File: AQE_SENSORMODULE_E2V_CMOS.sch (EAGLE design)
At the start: 29 parts, among them J1 440055-4, J2 AVR_SPI_PRG_6NS, U1 V_REG_LDOSMD, U2 V_REG_LDOSMD

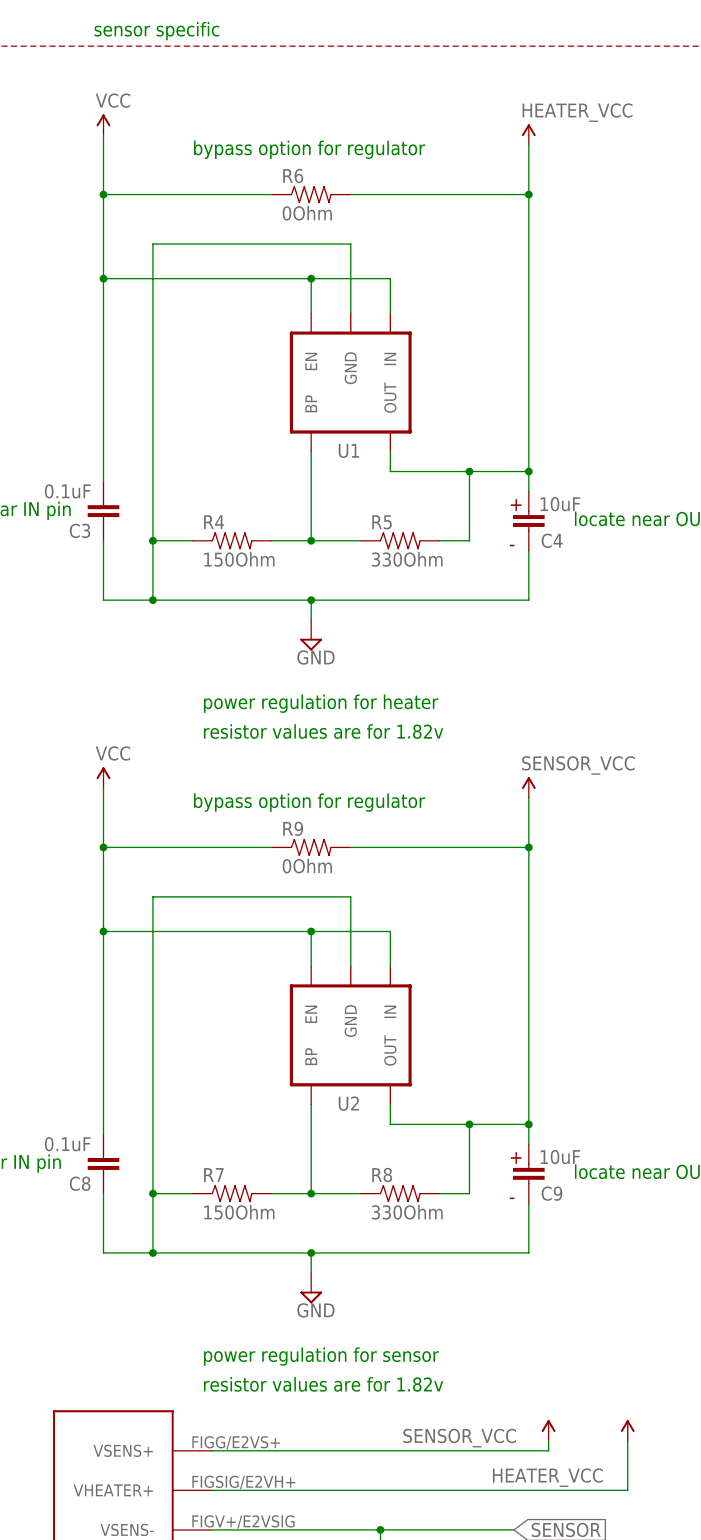
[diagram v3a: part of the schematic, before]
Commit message: minor changes in routing and component placement for improved decoupling, more representative values for resistors, and minor changes to silk screen
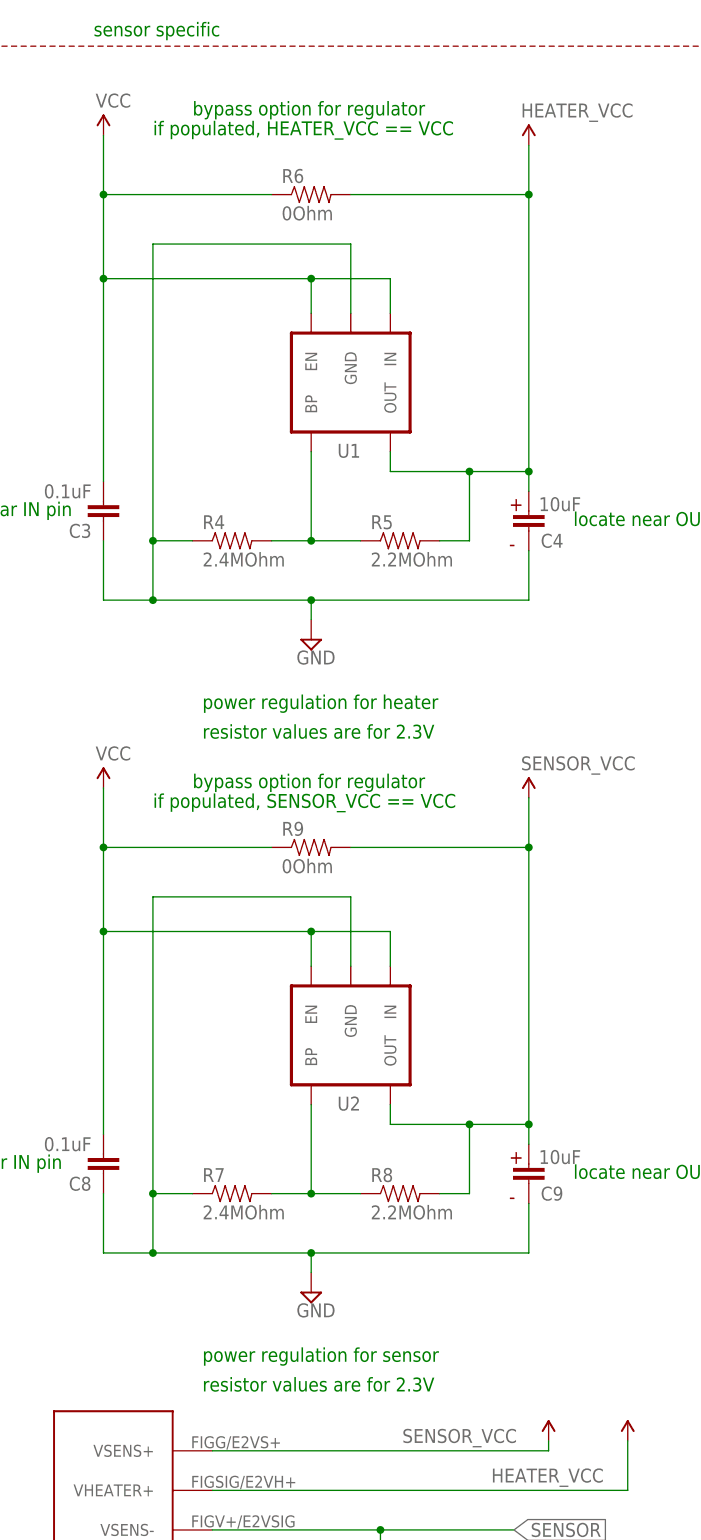
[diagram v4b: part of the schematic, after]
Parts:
- R4, R7: value 150Ohm -> 2.4MOhm
- R5, R8: value 330Ohm -> 2.2MOhm
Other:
- note added: "if populated, HEATER_VCC == VCC"
- note added: "if populated, SENSOR_VCC == VCC"
- note added: "resistor values are for 2.3V"
- note removed: "resistor values are for 1.82v"
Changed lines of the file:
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@@
 <setting verticaltext="up"/>
 </settings>
-<grid distance="0.05" unitdist="inch" unit="inch" style="lines" multiple="1" display="no" altdistance="0.01" altunitdist="inch" altunit="inch"/>
+<grid distance="0.1" unitdist="inch" unit="inch" style="lines" multiple="1" display="no" altdistance="0.01" altunitdist="inch" altunit="inch"/>
 <layers>
 <layer number="1" name="Top" color="4" fill="1" visible="no" active="no"/>
@@
 <part name="P+6" library="SparkFun" deviceset="VCC" device=""/>
 <part name="C6" library="SparkFun" deviceset="CAP" device="0603-CAP" value="0.1uF"/>
-<part name="R4" library="SparkFun" deviceset="RESISTOR" device="0805-RES" value="150Ohm"/>
-<part name="R5" library="SparkFun" deviceset="RESISTOR" device="0805-RES" value="330Ohm"/>
+<part name="R4" library="SparkFun" deviceset="RESISTOR" device="0805-RES" value="2.4MOhm"/>
+<part name="R5" library="SparkFun" deviceset="RESISTOR" device="0805-RES" value="2.2MOhm"/>
 <part name="C7" library="SparkFun" deviceset="CAP" device="0603-CAP" value="0.1uF"/>
 <part name="SUPPLY8" library="supply2" deviceset="GND" device=""/>
@@
 <part name="C9" library="wicked-device" deviceset="EEE-1EA100WR" device="" value="10uF"/>
 <part name="R9" library="SparkFun" deviceset="RESISTOR" device="0805-RES" value="0Ohm"/>
-<part name="R7" library="SparkFun" deviceset="RESISTOR" device="0805-RES" value="150Ohm"/>
-<part name="R8" library="SparkFun" deviceset="RESISTOR" device="0805-RES" value="330Ohm"/>
+<part name="R7" library="SparkFun" deviceset="RESISTOR" device="0805-RES" value="2.4MOhm"/>
+<part name="R8" library="SparkFun" deviceset="RESISTOR" device="0805-RES" value="2.2MOhm"/>
 <part name="U2" library="SparkFun" deviceset="V_REG_LDO" device="SMD"/>
 <part name="JP1" library="SparkFun" deviceset="STAND-OFF" device=""/>
@@
 <wire x1="152.4" y1="266.7" x2="40.64" y2="266.7" width="0.1524" layer="94" style="shortdash"/>
 <text x="67.31" y="267.97" size="1.778" layer="91">sensor specific</text>
-<text x="80.01" y="252.73" size="1.778" layer="91">bypass option for regulator</text>
+<text x="80.01" y="257.81" size="1.778" layer="91">bypass option for regulator</text>
 <text x="271.78" y="90.17" size="1.778" layer="91">programming header</text>
 <text x="76.2" y="12.7" size="1.778" layer="91">resistor values are sensor dependent</text>
@@
 <text x="158.75" y="120.65" size="1.778" layer="91">locate near VCC pin</text>
 <text x="124.46" y="207.01" size="1.778" layer="96">10uF</text>
-<text x="81.28" y="177.8" size="1.778" layer="91">resistor values are for 1.82v</text>
+<text x="81.28" y="177.8" size="1.778" layer="91">resistor values are for 2.3V</text>
 <text x="267.97" y="181.61" size="1.778" layer="91">locate near AREF pin</text>
 <text x="81.28" y="97.79" size="1.778" layer="91">power regulation for sensor</text>
-<text x="80.01" y="168.91" size="1.778" layer="91">bypass option for regulator</text>
+<text x="80.01" y="171.45" size="1.778" layer="91">bypass option for regulator</text>
 <text x="124.46" y="123.19" size="1.778" layer="96">10uF</text>
-<text x="81.28" y="93.98" size="1.778" layer="91">resistor values are for 1.82v</text>
+<text x="81.28" y="93.98" size="1.778" layer="91">resistor values are for 2.3V</text>
 <text x="45.085" y="206.375" size="1.778" layer="91">locate near IN pin</text>
 <text x="128.905" y="205.105" size="1.778" layer="91">locate near OUT pin</text>
@@
 <text x="128.905" y="121.285" size="1.778" layer="91">locate near OUT pin</text>
 <text x="359.41" y="146.685" size="1.778" layer="91">standoffs</text>
+<text x="74.93" y="255.27" size="1.778" layer="91">if populated, HEATER_VCC == VCC</text>
+<text x="74.93" y="168.91" size="1.778" layer="91">if populated, SENSOR_VCC == VCC</text>
 </plain>
 <instances>

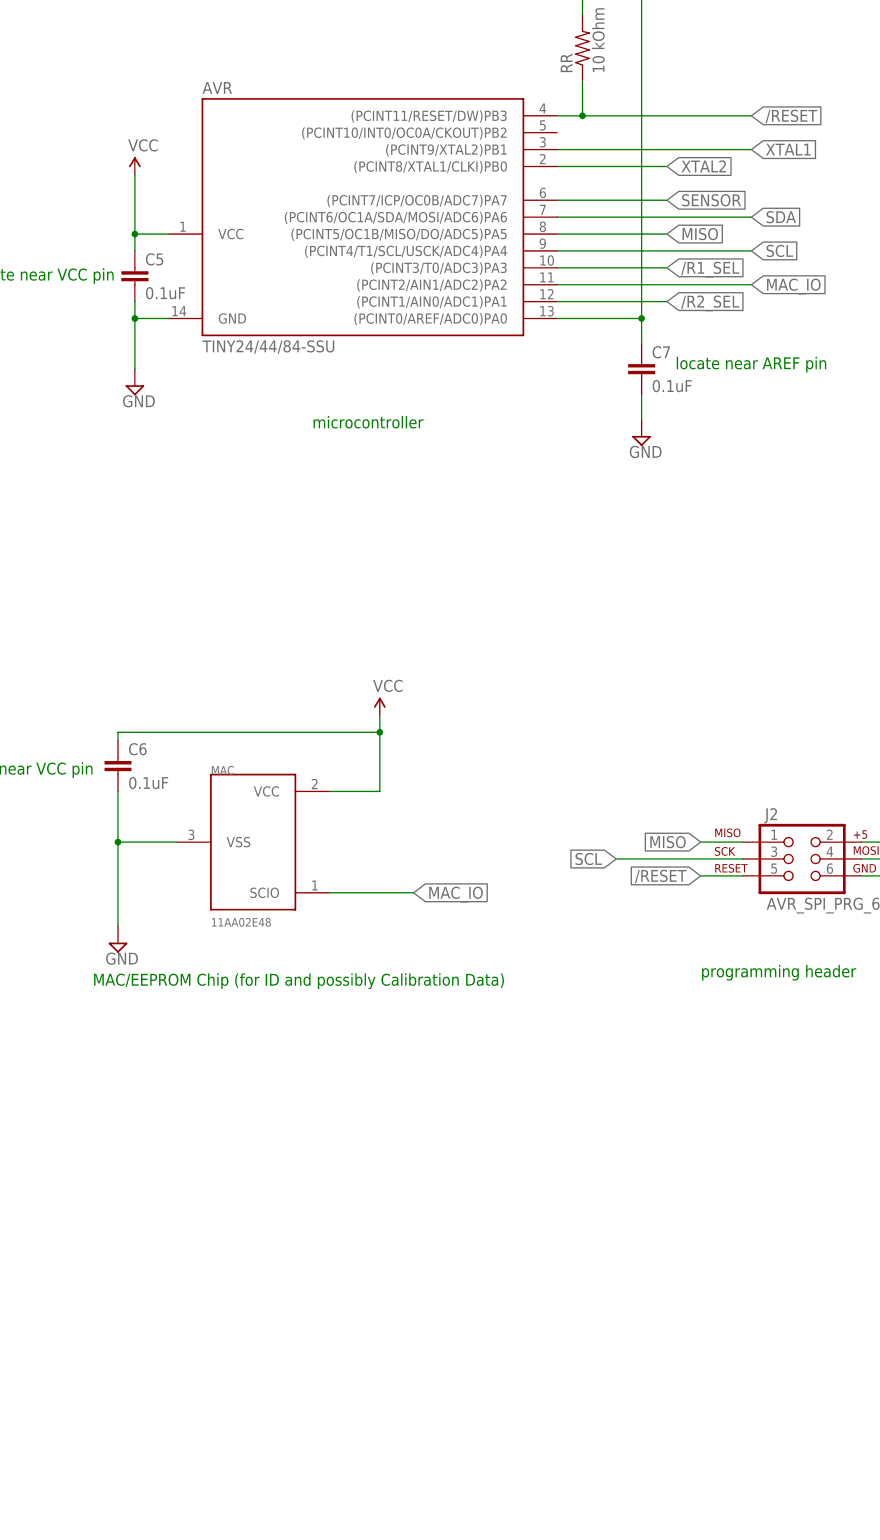
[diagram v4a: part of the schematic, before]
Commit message: last changes before switching heater approach to feedback controlled and changing microcontroller
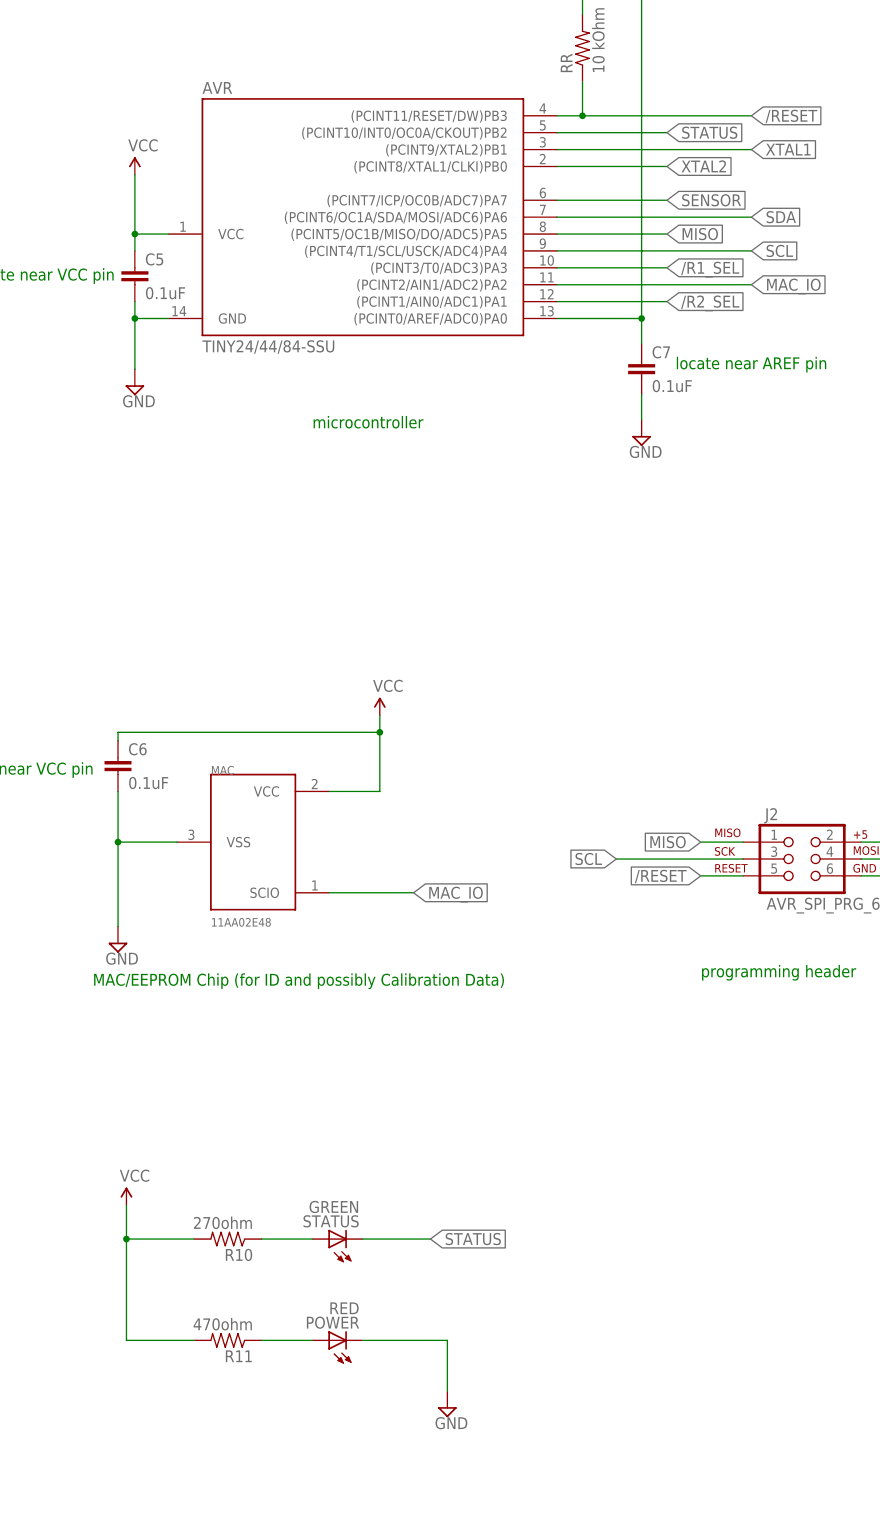
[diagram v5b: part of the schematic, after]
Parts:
- added POWER: RED, adafruit:LEDCHIPLED_0805
- added R10: 270ohm, SparkFun:RESISTOR0805-RES
- added R11: 470ohm, SparkFun:RESISTOR0805-RES
- added STATUS: GREEN, adafruit:LEDCHIPLED_0805
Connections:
- new net N$3: POWER.A, R11.1
- new net N$4: R10.1, STATUS.A
- new net STATUS: AVR.(PCINT10/INT0/OC0A/CKOUT)PB2, STATUS.C
- net GND: now also POWER.C
- net VCC: now also R10.2, R11.2
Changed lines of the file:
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@@
 <part name="JP1" library="SparkFun" deviceset="STAND-OFF" device=""/>
 <part name="JP2" library="SparkFun" deviceset="STAND-OFF" device=""/>
+<part name="STATUS" library="adafruit" deviceset="LED" device="CHIPLED_0805" value="GREEN"/>
+<part name="R10" library="SparkFun" deviceset="RESISTOR" device="0805-RES" value="270ohm"/>
+<part name="P+8" library="SparkFun" deviceset="VCC" device=""/>
+<part name="POWER" library="adafruit" deviceset="LED" device="CHIPLED_0805" value="RED"/>
+<part name="R11" library="SparkFun" deviceset="RESISTOR" device="0805-RES" value="470ohm"/>
+<part name="SUPPLY10" library="supply2" deviceset="GND" device=""/>
 </parts>
 <sheets>
@@
 <instance part="JP1" gate="G$1" x="361.95" y="152.4"/>
 <instance part="JP2" gate="G$1" x="369.57" y="152.4"/>
+<instance part="STATUS" gate="G$1" x="215.9" y="50.8" rot="R90"/>
+<instance part="R10" gate="G$1" x="200.66" y="50.8" rot="R180"/>
+<instance part="P+8" gate="1" x="185.42" y="55.88"/>
+<instance part="POWER" gate="G$1" x="215.9" y="35.56" rot="R90"/>
+<instance part="R11" gate="G$1" x="200.66" y="35.56" rot="R180"/>
+<instance part="SUPPLY10" gate="GND" x="233.68" y="25.4"/>
 </instances>
 <busses>
@@
 <junction x="95.25" y="153.035"/>
 <junction x="68.58" y="153.035"/>
+</segment>
+<segment>
+<pinref part="R10" gate="G$1" pin="2"/>
+<wire x1="195.58" y1="50.8" x2="185.42" y2="50.8" width="0.1524" layer="91"/>
+<wire x1="185.42" y1="50.8" x2="185.42" y2="55.88" width="0.1524" layer="91"/>
+<pinref part="P+8" gate="1" pin="VCC"/>
+<pinref part="R11" gate="G$1" pin="2"/>
+<wire x1="195.58" y1="35.56" x2="185.42" y2="35.56" width="0.1524" layer="91"/>
+<wire x1="185.42" y1="35.56" x2="185.42" y2="50.8" width="0.1524" layer="91"/>
+<junction x="185.42" y="50.8"/>
 </segment>
 </net>
@@
 <junction x="74.93" y="119.38"/>
 </segment>
+<segment>
+<pinref part="POWER" gate="G$1" pin="C"/>
+<wire x1="220.98" y1="35.56" x2="233.68" y2="35.56" width="0.1524" layer="91"/>
+<pinref part="SUPPLY10" gate="GND" pin="GND"/>
+<wire x1="233.68" y1="35.56" x2="233.68" y2="27.94" width="0.1524" layer="91"/>
+</segment>
 </net>
 <net name="/RESET" class="0">
@@
 </segment>
 </net>
+<net name="STATUS" class="0">
+<segment>
+<pinref part="AVR" gate="1" pin="(PCINT10/INT0/OC0A/CKOUT)PB2"/>
+<wire x1="250.19" y1="217.17" x2="266.7" y2="217.17" width="0.1524" layer="91"/>
+<label x="266.7" y="217.17" size="1.778" layer="95" xref="yes"/>
+</segment>
+<segment>
+<pinref part="STATUS" gate="G$1" pin="C"/>
+<wire x1="220.98" y1="50.8" x2="231.14" y2="50.8" width="0.1524" layer="91"/>
+<label x="231.14" y="50.8" size="1.778" layer="95" xref="yes"/>
+</segment>
+</net>
+<net name="N$4" class="0">
+<segment>
+<pinref part="R10" gate="G$1" pin="1"/>
+<pinref part="STATUS" gate="G$1" pin="A"/>
+<wire x1="205.74" y1="50.8" x2="213.36" y2="50.8" width="0.1524" layer="91"/>
+</segment>
+</net>
+<net name="N$3" class="0">
+<segment>
+<pinref part="R11" gate="G$1" pin="1"/>
+<pinref part="POWER" gate="G$1" pin="A"/>
+<wire x1="205.74" y1="35.56" x2="213.36" y2="35.56" width="0.1524" layer="91"/>
+</segment>
+</net>
